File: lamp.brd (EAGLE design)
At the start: 127.3 x 38.1 mm, 42 parts

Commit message: A bunch of layout and traces. Still need some support components for the microcontroller.
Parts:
- moved UC 60.3 mm to (50.8, 10.8), flipped to the bottom
- moved TA 57.9 mm to (63.2, 19.1), flipped to the bottom, turned to 0 degrees
- moved R10 10.2 mm to (10.2, 33.0), flipped to the bottom
- moved R6 9.84 mm to (60.6, 33.0), flipped to the bottom
- moved R7 9.84 mm to (47.9, 33.0), flipped to the bottom
- moved R8 9.84 mm to (35.2, 33.0), flipped to the bottom
- moved R9 9.84 mm to (22.5, 33.0), flipped to the bottom
- moved R5 2.54 mm to (66.0, 33.0), flipped to the bottom
- moved R4 2.54 mm to (78.7, 33.0), flipped to the bottom
- flipped R1 to the bottom
- flipped R2 to the bottom
- flipped R3 to the bottom
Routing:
- net +12V: track 0.00 -> 144.8 mm, vias 0 -> 1
- net N$39: track 121.9 -> 0.00 mm
- net N$35: track 0.00 -> 57.1 mm
- net N$34: track 0.00 -> 33.3 mm
- net N$37: track 0.00 -> 24.4 mm
- net N$38: track 0.00 -> 23.8 mm
- net N$33: track 0.00 -> 21.9 mm
- net N$36: track 0.00 -> 21.0 mm
- net N$22: track 0.00 -> 11.9 mm
- net N$30: track 0.00 -> 11.6 mm
- net N$27: track 0.00 -> 11.6 mm
- net N$24: track 0.00 -> 11.6 mm
- net N$21: track 0.00 -> 11.6 mm
- net N$18: track 0.00 -> 11.6 mm
- net N$15: track 0.00 -> 11.6 mm
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
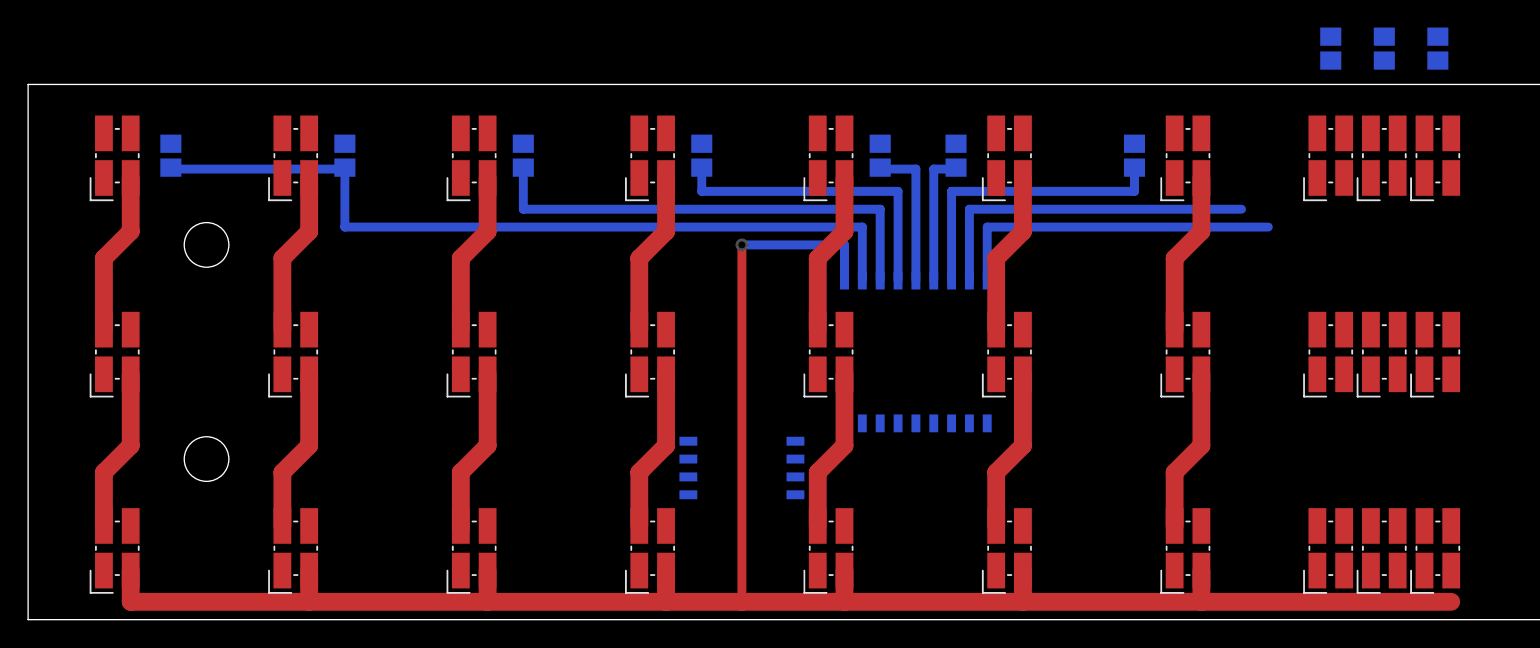
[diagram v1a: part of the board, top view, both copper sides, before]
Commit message: Added power supply for microcontroller, more routing, and some minor rearrangement on parts. Added solder pads for controller. Added ground plane for bottom.
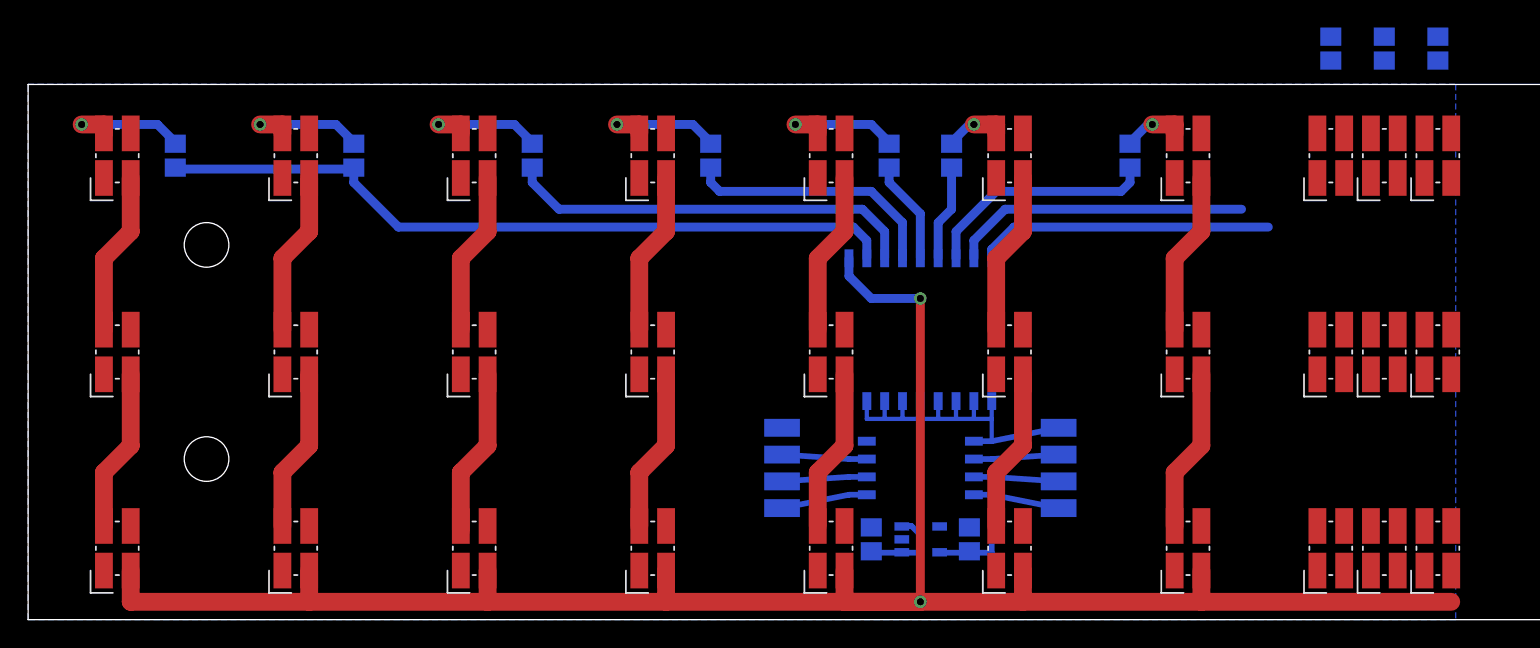
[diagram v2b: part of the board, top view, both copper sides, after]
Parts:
- removed U$19: CLA1BWKWMKW-4, lamp:PLCC4
- added C1, C2: (no value), Barebones-Arduino:0805
- added GND, PB0, PB1, PB2, PB3, PB4, PB5, VCC: (no value), wirepad:SMD1,27-2,54
- added LR: LP2985, lamp:SOT-23-5
- added U$1: CLA1BWKWMKW-4, lamp:PLCC4
- moved U$16 30.7 mm to (57.1, 5.08)
- moved U$15 14.0 mm to (69.8, 33.0)
- moved U$18 14.0 mm to (57.1, 33.0)
- moved U$14 14.0 mm to (69.8, 19.1)
- moved U$17 14.0 mm to (57.1, 19.1)
- moved UC 12.7 mm to (63.5, 10.8), turned to 90 degrees
- moved TA 1.62 mm to (63.5, 20.6)
- moved R6 0.64 mm to (61.3, 33.0)
- moved R7 0.63 mm to (48.6, 33.0)
- moved R8 0.63 mm to (35.9, 33.0)
- moved R9 0.63 mm to (23.2, 33.0)
- moved R5 0.32 mm to (65.7, 33.0)
- moved R10 0.32 mm to (10.5, 33.0)
- moved R4 0.32 mm to (78.4, 33.0)
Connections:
- new net GND: C1.2, C2.2, GND.1, LR.P$2, TA.P$9, UC.P$4
- new net N$13: R6.2, U$18.P$4
- new net N$16: U$16.P$4, U$17.P$2
- new net N$31: U$1.P$4, U$14.P$2
- new net N$39: PB3.1, UC.P$2
- new net N$43: R5.2, U$15.P$4
- new net N$44: PB4.1, UC.P$3
- new net N$47: PB0.1, TA.P$1, TA.P$2, TA.P$3, TA.P$4, TA.P$5, TA.P$6, TA.P$7, TA.P$8, UC.P$5
- net +12V: now also C1.1, LR.P$1, LR.P$3, U$1.P$2, U$16.P$2; no longer U$14.P$2, U$17.P$2
- net N$14: now also PB1.1, UC.P$6; no longer R5.2, U$16.P$4
- net N$15: now also C2.1, LR.P$5, UC.P$8, VCC.1; no longer U$15.P$4, U$16.P$2
- net N$17: now also PB2.1, UC.P$7; no longer R6.2, U$19.P$4
- net N$18: now also PB5.1, UC.P$1; no longer U$18.P$4, U$19.P$2
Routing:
- net N$47: track 0.00 -> 26.8 mm
- net N$31: track 0.00 -> 11.6 mm
- net N$16: track 0.00 -> 11.6 mm
- net N$20: track 0.00 -> 9.42 mm, vias 0 -> 1
- net N$13: track 0.00 -> 9.42 mm, vias 0 -> 1
- net N$29: track 0.00 -> 9.42 mm, vias 0 -> 1
- net N$26: track 0.00 -> 9.42 mm, vias 0 -> 1
- net N$23: track 0.00 -> 9.42 mm, vias 0 -> 1
- net +12V: track 144.8 -> 153.3 mm, vias 1 -> 2
- net N$44: track 0.00 -> 6.04 mm
- net N$39: track 0.00 -> 6.04 mm
- net N$17: track 0.00 -> 6.04 mm
- net N$14: track 0.00 -> 6.04 mm
- net N$18: track 11.6 -> 6.13 mm
- net N$11: track 0.00 -> 4.34 mm, vias 0 -> 1
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- added copper zone on layer 16, net N$45

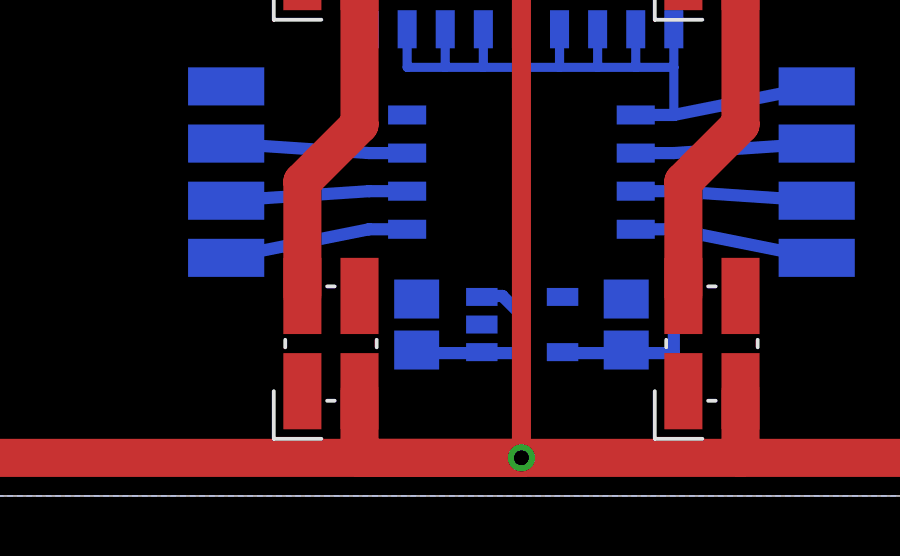
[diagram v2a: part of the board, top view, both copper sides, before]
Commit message: Fixed a broken ground on the voltage regulator
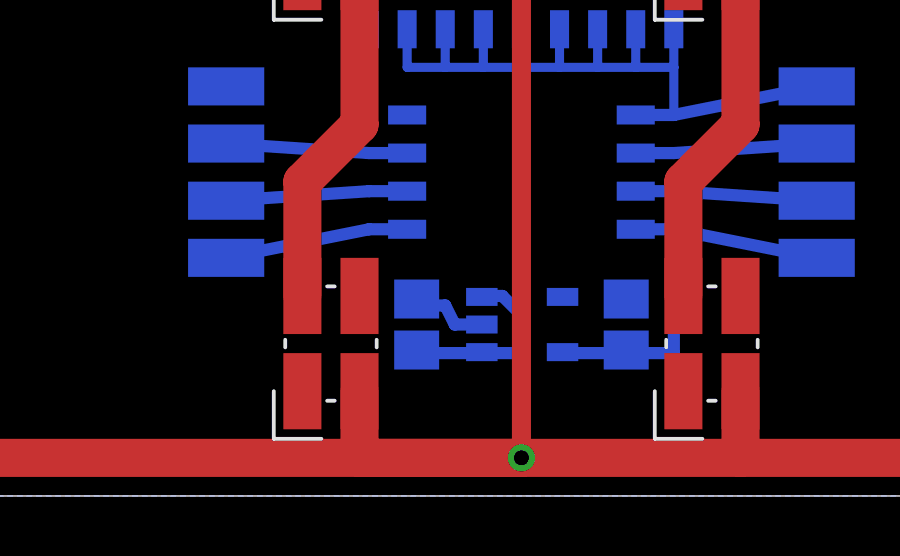
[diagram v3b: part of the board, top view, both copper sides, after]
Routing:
- net GND: track 0.00 -> 2.61 mm
- added copper zone on layer 16, net GND
- removed copper zone on layer 16, net N$45
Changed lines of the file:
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@@
 <contactref element="GND" pad="1"/>
 <contactref element="UC" pad="P$4"/>
-<wire x1="59.69" y1="12.7" x2="58.42" y2="15.5575" width="0" layer="19" extent="16-16"/>
-<wire x1="53.6575" y1="13.6525" x2="58.42" y2="15.5575" width="0" layer="19" extent="16-16"/>
-<wire x1="60.0075" y1="6.565" x2="59.69" y2="12.7" width="0" layer="19" extent="16-16"/>
-<wire x1="62.18" y1="5.715" x2="60.0075" y2="6.565" width="0" layer="19" extent="16-16"/>
-<wire x1="66.9925" y1="6.565" x2="62.18" y2="5.715" width="0" layer="19" extent="16-16"/>
+<polygon width="0.254" layer="16" isolate="0.4064">
+<vertex x="0" y="0"/>
+<vertex x="0" y="38.1"/>
+<vertex x="101.6" y="38.1"/>
+<vertex x="101.6" y="0"/>
+</polygon>
+<wire x1="60.0075" y1="6.35" x2="60.96" y2="6.35" width="0.4064" layer="16"/>
+<wire x1="60.96" y1="6.35" x2="61.2775" y2="5.715" width="0.4064" layer="16"/>
+<wire x1="61.2775" y1="5.715" x2="62.23" y2="5.715" width="0.4064" layer="16"/>
 </signal>
 <signal name="N$14">
@@
 <wire x1="64.87" y1="4.795" x2="64.77" y2="4.7625" width="0" layer="19" extent="16-16"/>
 </signal>
-<signal name="N$45">
-<polygon width="0.254" layer="16" isolate="0.4064">
-<vertex x="0" y="0"/>
-<vertex x="0" y="38.1"/>
-<vertex x="101.6" y="38.1"/>
-<vertex x="101.6" y="0"/>
-</polygon>
-</signal>
 </signals>

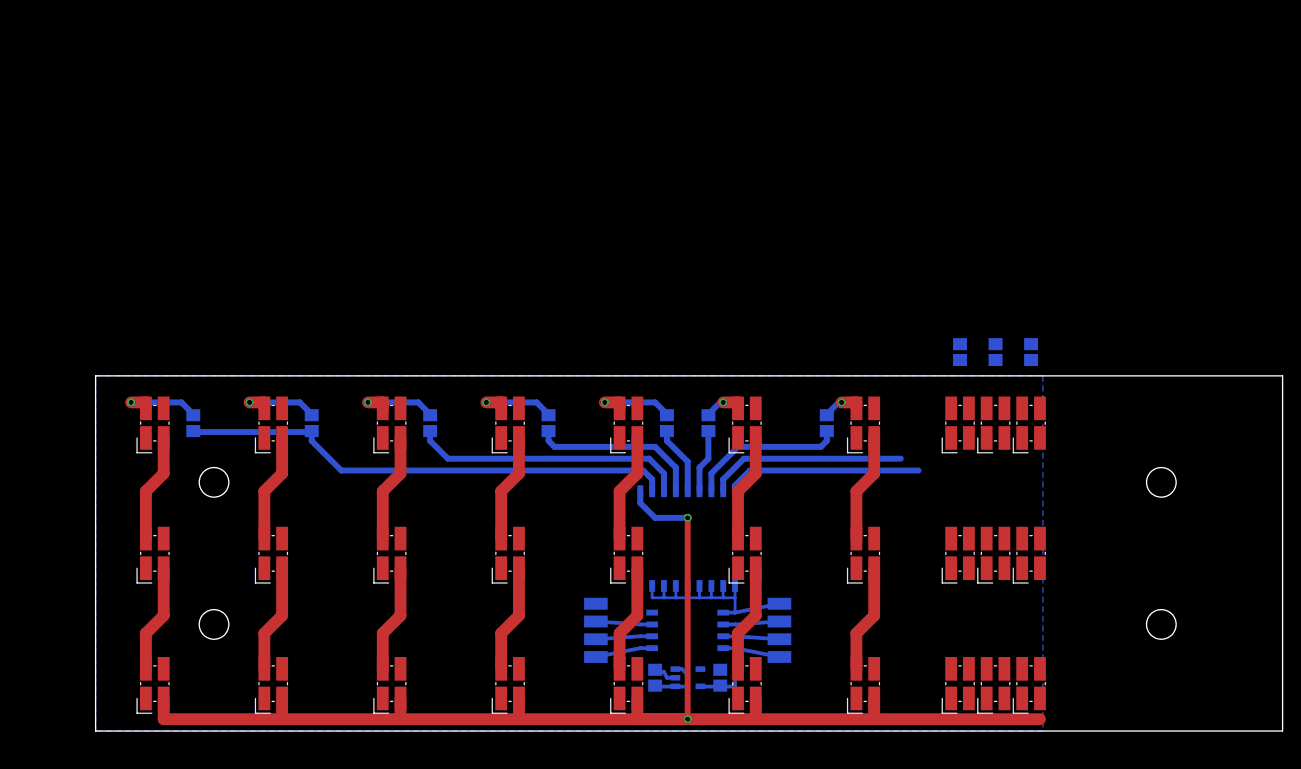
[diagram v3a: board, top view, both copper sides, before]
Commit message: Finished top layer: added heat sink flags on the leds, filled in the ground plane, did some more routing. Because I'm on babby's first eagle license, I can't place the last 8 parts, but all the routing at that end is done and the parts are space correctly relative to each other, they just need to be move into place as a single group.
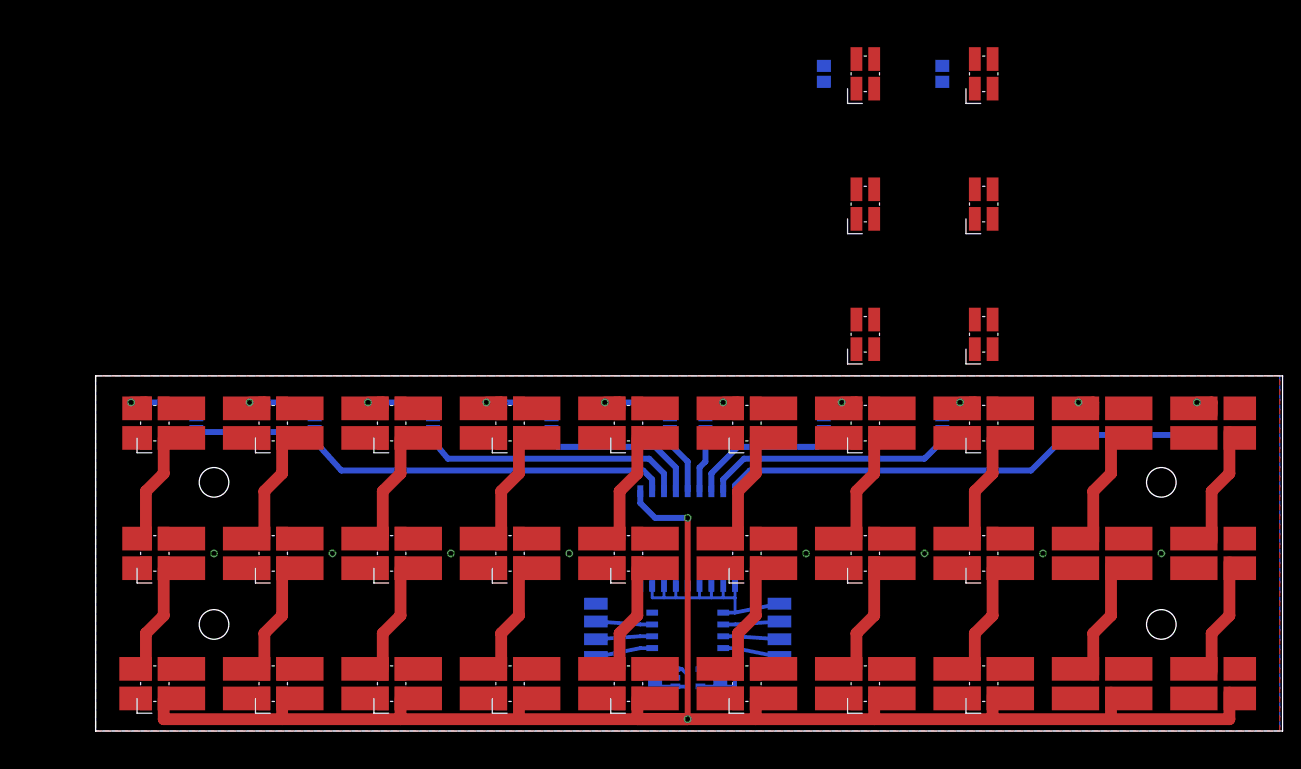
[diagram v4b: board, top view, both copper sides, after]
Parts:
- moved U$2 40.0 mm to (82.5, 42.5)
- moved U$3 40.0 mm to (82.5, 56.5)
- moved U$4 40.0 mm to (82.5, 70.5)
- moved U$5 37.8 mm to (95.2, 42.5)
- moved U$6 37.8 mm to (95.2, 56.5)
- moved U$7 37.8 mm to (95.2, 70.5)
- moved R1 35.1 mm to (78.1, 70.5)
- moved R2 31.3 mm to (90.8, 70.5)
- moved R3 7.85 mm to (90.8, 33.0)
- moved U$10 2.54 mm to (95.2, 33.0)
- moved U$8 2.54 mm to (95.2, 5.08)
- moved U$9 2.54 mm to (95.2, 19.1)
- moved R7 0.32 mm to (48.9, 33.0)
- moved R8 0.32 mm to (36.2, 33.0)
- moved R9 0.32 mm to (23.5, 33.0)
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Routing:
- net N$38: track 21.0 -> 50.9 mm
- net +12V: track 153.3 -> 179.0 mm
- net N$50: track 0.00 -> 12.5 mm
- net N$53: track 0.00 -> 12.5 mm
- net N$49: track 0.00 -> 12.5 mm
- net N$54: track 0.00 -> 12.2 mm
- net N$9: track 0.00 -> 11.6 mm
- net N$7: track 0.00 -> 11.6 mm
- net N$37: track 21.2 -> 27.4 mm
- net N$51: track 0.00 -> 5.29 mm, vias 0 -> 1
- net N$45: track 0.00 -> 5.29 mm, vias 0 -> 1
- net N$8: track 0.00 -> 4.65 mm, vias 0 -> 1
- net N$52: track 0.00 -> 2.22 mm
- net GND: vias 0 -> 8
- added copper zone on layer 1, net GND
